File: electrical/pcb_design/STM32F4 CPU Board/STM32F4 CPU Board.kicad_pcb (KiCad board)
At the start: 2 copper layers, 82.5 x 82.5 mm, 37 parts, among them J1 STLINK_STDC14, J2 STLINK_TagConnect_6, J3 Conn_01x15_Pin, J4 Conn_01x15_Pin, M1 M3, M2 M3, M3 M3, M4 M3, U1 STM32F405RGT6, U2 AMS1117-3.3, Y1 16MHz

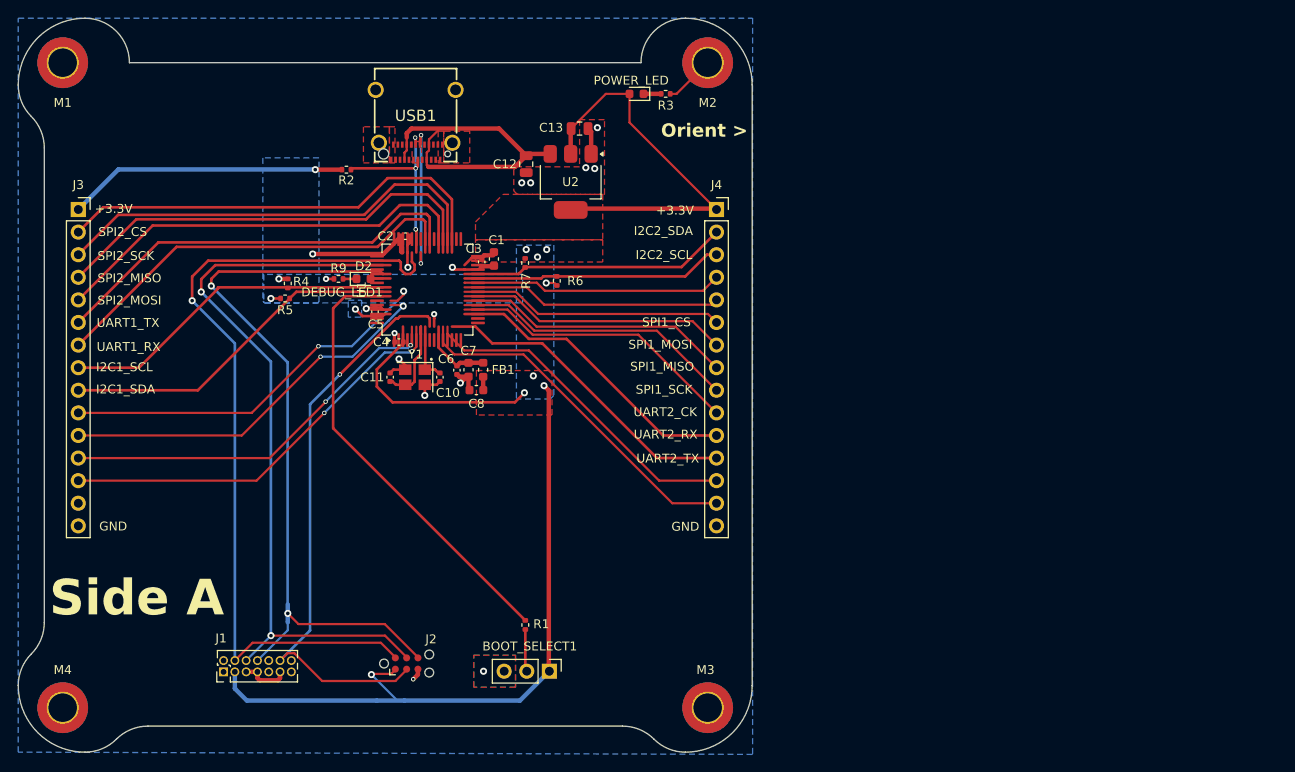
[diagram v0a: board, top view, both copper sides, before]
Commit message: Starting layout of STM32F4 CPU board
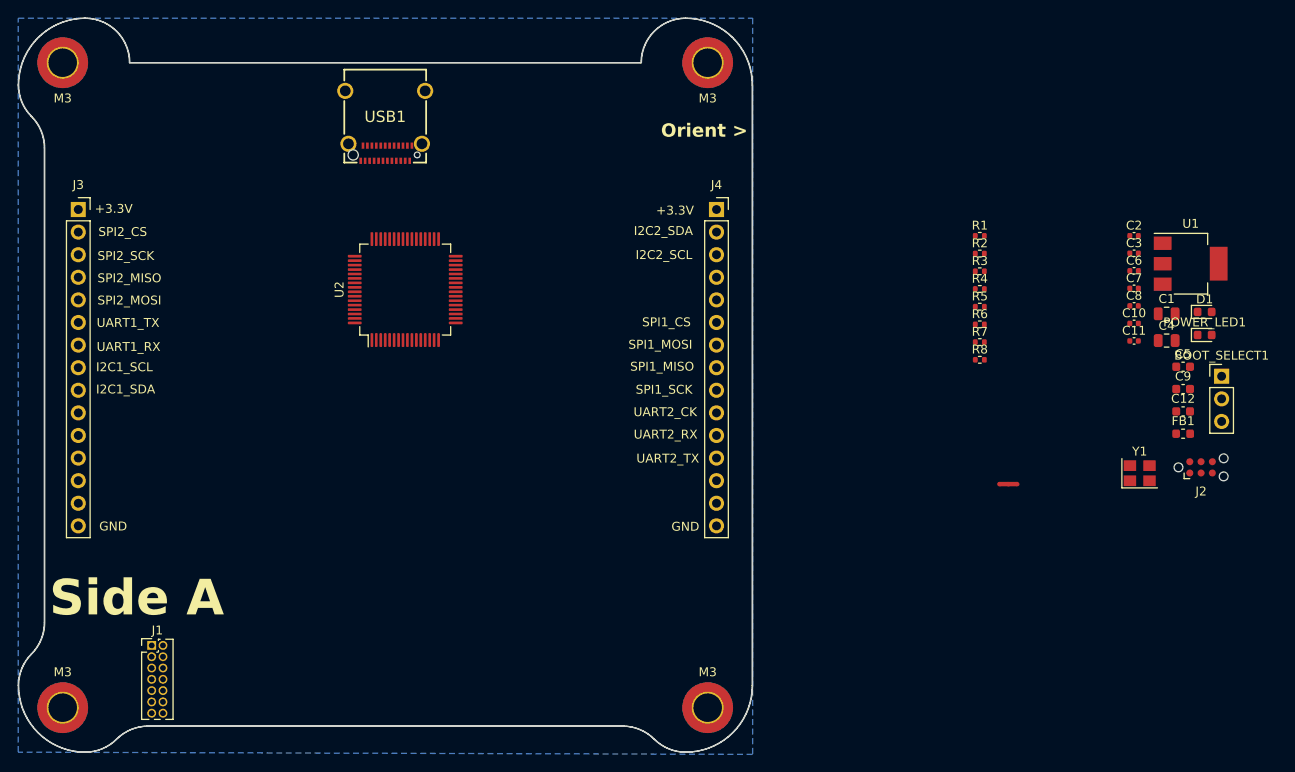
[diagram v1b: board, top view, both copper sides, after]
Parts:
- removed C13: 22u, Capacitor_SMD:C_0805_2012Metric
- removed D2: DEBUG_LED1, LED_SMD:LED_0603_1608Metric
- removed M1, M2, M3, M4: M3, MountingHole:MountingHole_3.2mm_M3_ISO7380_Pad_TopBottom
- removed R9: 1k5, Resistor_SMD:R_0402_1005Metric
- added C9: 1u, Capacitor_SMD:C_0603_1608Metric, F.Cu at (230.9, 109.2)
- added D1: DEBUG_LED1, LED_SMD:LED_0603_1608Metric, F.Cu at (233.4, 100.5)
- added PCB1: ~, footprints:PCB_Shape, F.Cu at (100.0, 150.0)
- added R8: 10k, Resistor_SMD:R_0402_1005Metric, F.Cu at (208.1, 105.9)
- C1: value 10u -> 22u; footprint Capacitor_SMD:C_0603_1608Metric -> Capacitor_SMD:C_0805_2012Metric
- C10, C11: value 10p -> 100n
- C12: value 22u -> 1u; footprint Capacitor_SMD:C_0805_2012Metric -> Capacitor_SMD:C_0603_1608Metric
- C2, C3: value 100n -> 10p
- C4: value 100n -> 22u; footprint Capacitor_SMD:C_0402_1005Metric -> Capacitor_SMD:C_0805_2012Metric
- C5: value 100n -> 10u; footprint Capacitor_SMD:C_0402_1005Metric -> Capacitor_SMD:C_0603_1608Metric
- C6: value 10n -> 100n
- C7: value 1u -> 10n; footprint Capacitor_SMD:C_0603_1608Metric -> Capacitor_SMD:C_0402_1005Metric
- C8: value 1u -> 100n; footprint Capacitor_SMD:C_0603_1608Metric -> Capacitor_SMD:C_0402_1005Metric
- NT1: moved to F.Cu
- R1: value 10k -> 1k5
- U1: value STM32F405RGT6 -> AMS1117-3.3; footprint Package_QFP:LQFP-64_10x10mm_P0.5mm -> Package_TO_SOT_SMD:SOT-223-3_TabPin2
- U2: value AMS1117-3.3 -> STM32F405RGT6; footprint Package_TO_SOT_SMD:SOT-223-3_TabPin2 -> Package_QFP:LQFP-64_10x10mm_P0.5mm
- moved J2 92.0 mm to (233.0, 118.0)
- moved C5 91.0 mm to (230.9, 106.7), turned to 0 degrees
- moved C4 86.3 mm to (229.1, 103.7), turned to 0 degrees
- moved U1 85.8 mm to (231.8, 95.1), turned to 0 degrees
- moved C11 83.7 mm to (225.4, 103.8), turned to 0 degrees
- moved BOOT_SELECT1 82.5 mm to (235.3, 107.7), turned to 0 degrees
- moved NT1 82.3 mm to (211.3, 119.9), turned to 0 degrees
- moved Y1 82.2 mm to (226.1, 118.6), turned to 0 degrees
- moved C2 81.9 mm to (225.4, 92.0)
- moved FB1 79.0 mm to (230.9, 114.2), turned to 0 degrees
- moved C12 78.9 mm to (230.9, 111.7), turned to 0 degrees
- moved C10 78.3 mm to (225.4, 101.8), turned to 0 degrees
- moved R5 78.1 mm to (208.1, 99.9)
- moved R4 77.8 mm to (208.1, 97.9), turned to 0 degrees
- moved C6 76.9 mm to (225.4, 95.9), turned to 0 degrees
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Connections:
- C1 pad 1: +3.3V -> VBUS
- C10 pad 1: HSE_IN -> +3.3V
- C11 pad 1: HSE_OUT -> +3.3V
- C12 pad 1: VBUS -> +3.3V
- C2 pad 1: +3.3V -> HSE_IN
- C3 pad 1: +3.3V -> HSE_OUT
- C6 pad 1: +3.3VA -> +3.3V
- R1 pad 1: /sw_boot0 -> +3.3V
- R1 pad 2: /BOOT0 -> USB_D+
- R2 pad 1: +3.3V -> /PWR_LED_K
- R2 pad 2: USB_D+ -> GND
- R3 pad 1: /PWR_LED_K -> +3.3V
- R3 pad 2: GND -> I2C1_SCL
- R4 pad 2: I2C1_SCL -> I2C2_SCL
- R6 pad 2: I2C2_SCL -> I2C2_SDA
- R7 pad 1: +3.3V -> /DEBUG_LED_K
- R7 pad 2: I2C2_SDA -> GND
- U1 pad 1: unconnected-(U1-VBAT-Pad1) -> GND
- U1 pad 2: unconnected-(U1-PC13-Pad2) -> +3.3V
- U1 pad 3: unconnected-(U1-PC14-Pad3) -> VBUS
- U2 pad 1: GND -> unconnected-(U2-VBAT-Pad1)
- U2 pad 2: +3.3V -> unconnected-(U2-PC13-Pad2)
- U2 pad 3: VBUS -> unconnected-(U2-PC14-Pad3)
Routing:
- net +3.3V: track 207.5 -> 0.14 mm, vias 13 -> 0
- net SWDIO: track 93.9 -> 0.00 mm, vias 1 -> 0
- net SWCLK: track 85.6 -> 0.00 mm, vias 2 -> 0
- net PWM_1: track 65.3 -> 0.00 mm
- net NRST: track 65.3 -> 0.00 mm, vias 1 -> 0
- net SW0: track 60.8 -> 0.00 mm, vias 1 -> 0
- net SPI2_CS: track 51.5 -> 0.00 mm
- net SPI2_SCK: track 51.1 -> 0.00 mm
- net /BOOT0: track 51.0 -> 0.00 mm
- net SPI2_MISO: track 50.4 -> 0.00 mm
- net SPI2_MOSI: track 49.5 -> 0.00 mm
- net UART1_TX: track 48.8 -> 0.00 mm
- net UART1_RX: track 48.4 -> 0.00 mm
- net PWM_5: track 46.5 -> 0.00 mm, vias 2 -> 0
- net PWM_4: track 44.8 -> 0.00 mm, vias 2 -> 0
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- removed copper zone on B.Cu, net +3.3V
- removed copper zone on F.Cu, net +3.3V
- removed copper zone on F.Cu, net GND
- removed copper zone on F.Cu, net USB_D-
